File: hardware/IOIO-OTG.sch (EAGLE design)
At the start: 60 parts, among them Q1 IRLML2244, Q2 2N7002PW, Q3 AO3404A, U1 PIC24FJ256GB206, U2 TPS62133RGTT, U3 V_REG_MIC5216

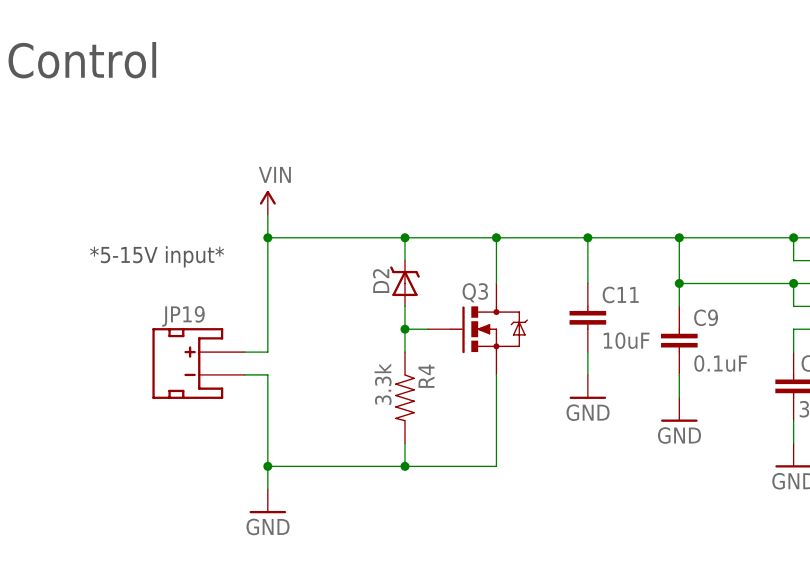
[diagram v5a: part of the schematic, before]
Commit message: Package update on D2 (zener) and PROD_IDs
Had to scoot upwards on most of the power circuit components to make
space for the correct package size on the zener.

All PROD_IDs done.
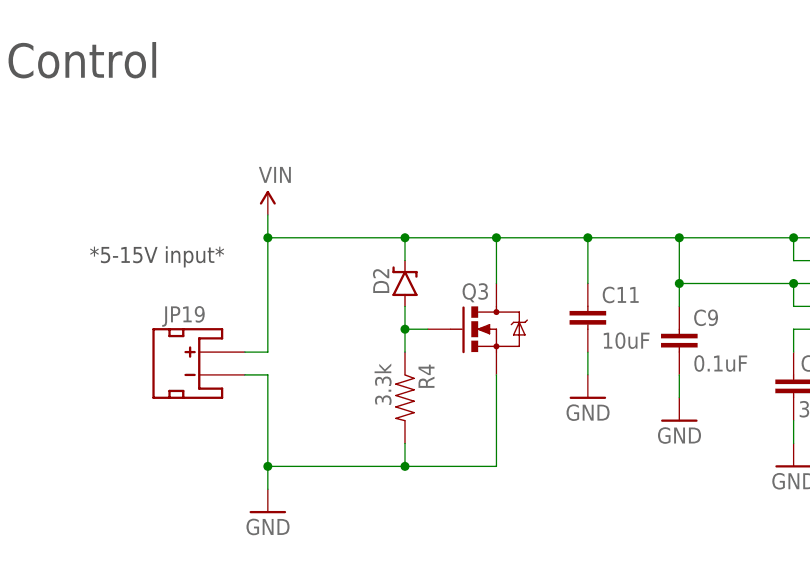
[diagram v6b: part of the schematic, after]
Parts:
- D2: device IOIO-OTG:SPARKFUN-DISCRETESEMI_DIODE-SCHOTTKY -> SparkFun-DiscreteSemi:DIODE-ZENERDZ2J150M0L
- Q3: value AO3404A -> MOSFET-NCHANNELAO3404A; device IOIO-OTG:SPARKFUN-DISCRETESEMI_MOSFET-NCHANNELSMD -> SparkFun-DiscreteSemi:MOSFET-NCHANNELAO3404A; PART# DMN3404L -> AO3404A
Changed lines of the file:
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@@
 <part name="TP3" library="SparkFun-Passives" deviceset="TEST-POINT" device="3"/>
 <part name="U$6" library="SparkFun-Aesthetics" deviceset="IOIO-OTG" device=""/>
-<part name="Q3" library="IOIO-OTG" deviceset="SPARKFUN-DISCRETESEMI_MOSFET-NCHANNEL" device="SMD" value="AO3404A">
-<attribute name="PART#" value="DMN3404L"/>
+<part name="Q3" library="SparkFun-DiscreteSemi" deviceset="MOSFET-NCHANNEL" device="AO3404A" value="MOSFET-NCHANNELAO3404A">
+<attribute name="PART#" value="AO3404A"/>
 </part>
 <part name="R4" library="SparkFun-Resistors" deviceset="3.3KOHM1/10W1%(0603)" device="" value="3.3k"/>
-<part name="D2" library="IOIO-OTG" deviceset="SPARKFUN-DISCRETESEMI_DIODE-SCHOTTKY" device="" value="DZ2J160M0L">
+<part name="D2" library="SparkFun-DiscreteSemi" deviceset="DIODE-ZENER" device="DZ2J150M0L" value="DZ2J160M0L">
 <attribute name="PART#" value="DZ2J150M0L"/>
 </part>

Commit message: Schematic Cleanup
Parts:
- JP1: value VIN -> (none)
- JP2: value 3.3V -> (none)
- JP4: value 5V -> (none)
- U3: value V_REG_MIC5216 -> MIC5216
